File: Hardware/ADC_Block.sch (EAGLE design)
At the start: 33 parts, among them U1 ADS1015, U2 PCA9306, U3 3.3V

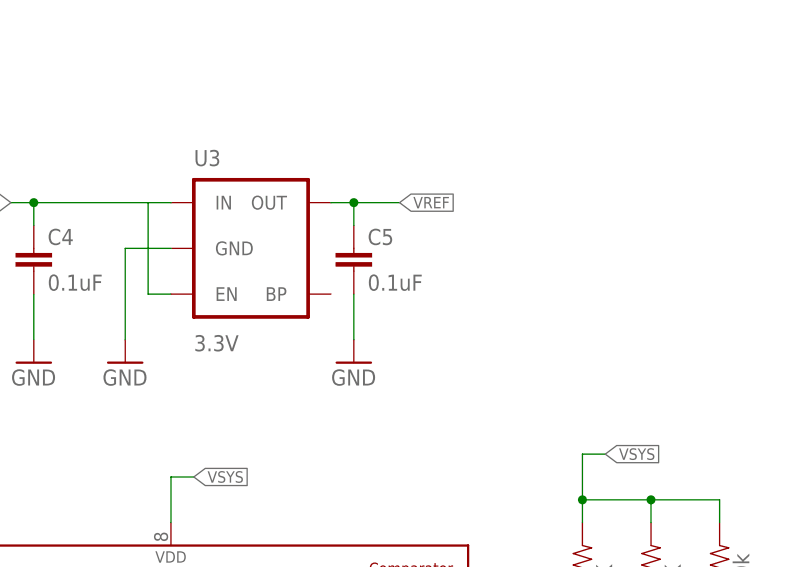
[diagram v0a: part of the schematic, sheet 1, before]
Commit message: replaces output capacitor on the 3.3v regulator with 2.2uF
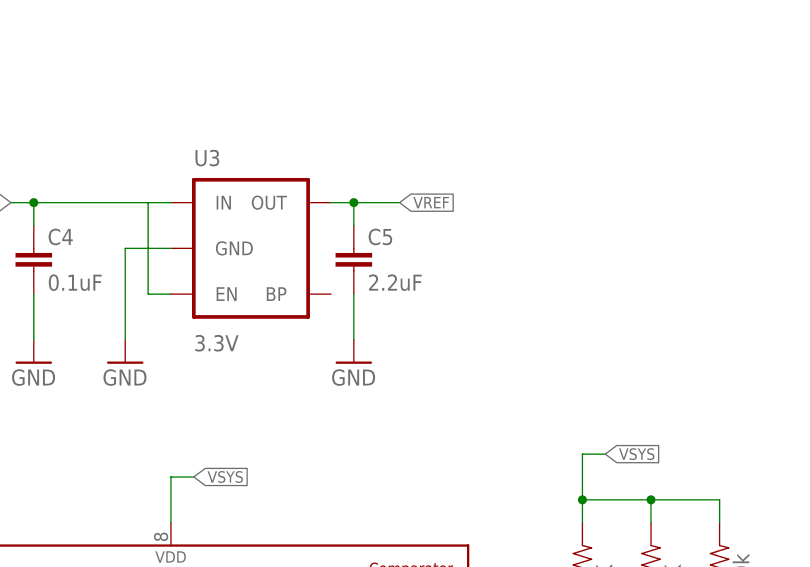
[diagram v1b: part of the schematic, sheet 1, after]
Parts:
- C5: value 0.1uF -> 2.2uF; device SparkFun-Capacitors:0.1UF-25V(+80/-20%)(0603) -> SparkFun-Capacitors:2.2UF-10V-20%(0603)
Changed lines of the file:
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@@
 <?xml version="1.0" encoding="utf-8"?>
 <!DOCTYPE eagle SYSTEM "eagle.dtd">
-<eagle version="7.3.0">
+<eagle version="7.1.0">
 <drawing>
 <settings>
@@
 <part name="U3" library="SparkFun-PowerIC" deviceset="MIC5205" device="3.3V" value="3.3V"/>
 <part name="C4" library="SparkFun-Capacitors" deviceset="0.1UF-25V(+80/-20%)(0603)" device="" value="0.1uF"/>
-<part name="C5" library="SparkFun-Capacitors" deviceset="0.1UF-25V(+80/-20%)(0603)" device="" value="0.1uF"/>
+<part name="C5" library="SparkFun-Capacitors" deviceset="2.2UF-10V-20%(0603)" device="" value="2.2uF"/>
 <part name="GND8" library="SparkFun-Aesthetics" deviceset="GND" device=""/>
 <part name="GND9" library="SparkFun-Aesthetics" deviceset="GND" device=""/>

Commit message: fixed thermal issue preventing gnd pour to connect with pads
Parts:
- FRAME1, FRAME2: value (none) -> FRAME-LETTER

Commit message: updated part values
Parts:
- R1, R2: device SparkFun-Resistors:10KOHM1/10W1%(0603)0603 -> SparkFun-Resistors:10KOHM-1/10W-1%(0603)0603
- R4, R5, R6: device SparkFun-Resistors:2.2KOHM1/10W1%(0603) -> SparkFun-Resistors:2.2KOHM-1/10W-1%(0603)
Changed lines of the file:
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@@
 <part name="C1" library="SparkFun-Capacitors" deviceset="0.1UF-25V(+80/-20%)(0603)" device="" value="0.1uF"/>
 <part name="U1" library="SparkFun-AnalogIC" deviceset="ADS1015" device="" value="ADS1015"/>
-<part name="R1" library="SparkFun-Resistors" deviceset="10KOHM1/10W1%(0603)" device="0603" value="10K"/>
-<part name="R2" library="SparkFun-Resistors" deviceset="10KOHM1/10W1%(0603)" device="0603" value="10K"/>
+<part name="R1" library="SparkFun-Resistors" deviceset="10KOHM-1/10W-1%(0603)" device="0603" value="10K"/>
+<part name="R2" library="SparkFun-Resistors" deviceset="10KOHM-1/10W-1%(0603)" device="0603" value="10K"/>
 <part name="U2" library="SparkFun-DigitalIC" deviceset="PCA9306" device="PCA9306DC-1:1" value="PCA9306"/>
 <part name="SUPPLY1" library="SparkFun-Aesthetics" deviceset="1.8V" device=""/>
@@
 <part name="SUPPLY4" library="SparkFun-Aesthetics" deviceset="1.8V" device=""/>
 <part name="R3" library="SparkFun-Resistors" deviceset="200KOHM1/10W1%(0603)" device="200K" value="200k"/>
-<part name="R4" library="SparkFun-Resistors" deviceset="2.2KOHM1/10W1%(0603)" device="" value="DNP"/>
-<part name="R5" library="SparkFun-Resistors" deviceset="2.2KOHM1/10W1%(0603)" device="" value="DNP"/>
+<part name="R4" library="SparkFun-Resistors" deviceset="2.2KOHM-1/10W-1%(0603)" device="" value="DNP"/>
+<part name="R5" library="SparkFun-Resistors" deviceset="2.2KOHM-1/10W-1%(0603)" device="" value="DNP"/>
 <part name="GND2" library="SparkFun-Aesthetics" deviceset="GND" device=""/>
 <part name="GND5" library="SparkFun-Aesthetics" deviceset="GND" device=""/>
@@
 <part name="LOGO1" library="SparkFun-Aesthetics" deviceset="SFE_LOGO_NAME_FLAME" device=".1_INCH"/>
 <part name="LOGO4" library="SparkFun-Aesthetics" deviceset="OSHW-LOGO" device="S"/>
-<part name="R6" library="SparkFun-Resistors" deviceset="2.2KOHM1/10W1%(0603)" device="" value="2.2k"/>
+<part name="R6" library="SparkFun-Resistors" deviceset="2.2KOHM-1/10W-1%(0603)" device="" value="2.2k"/>
 <part name="FID1" library="SparkFun-Aesthetics" deviceset="FIDUCIAL" device="1X2" value="FIDUCIAL1X2"/>
 <part name="FID2" library="SparkFun-Aesthetics" deviceset="FIDUCIAL" device="1X2" value="FIDUCIAL1X2"/>
@@
 <junction x="78.74" y="149.86"/>
 <label x="76.2" y="149.86" size="1.27" layer="95" rot="R180" xref="yes"/>
+<junction x="91.44" y="149.86"/>
 </segment>
 </net>
@@
 </sheet>
 </sheets>
+<errors>
+</errors>
 </schematic>
 </drawing>

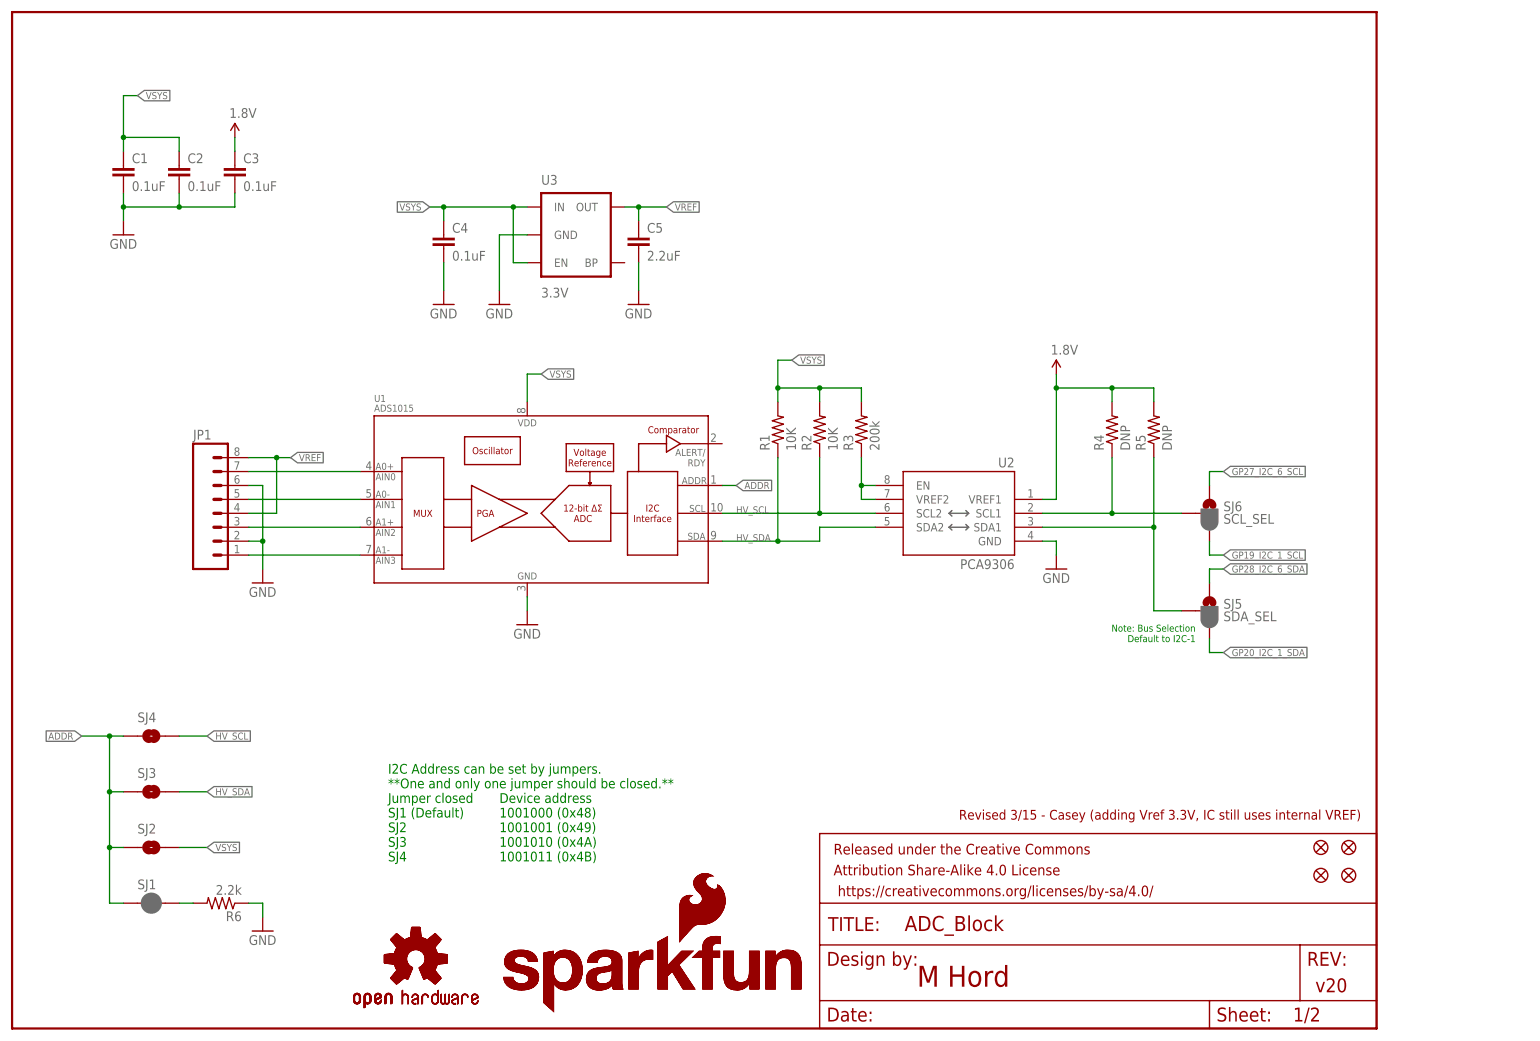
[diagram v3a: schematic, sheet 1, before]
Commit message: Added resistor to output cap on LDO. Changed header to locking male header.
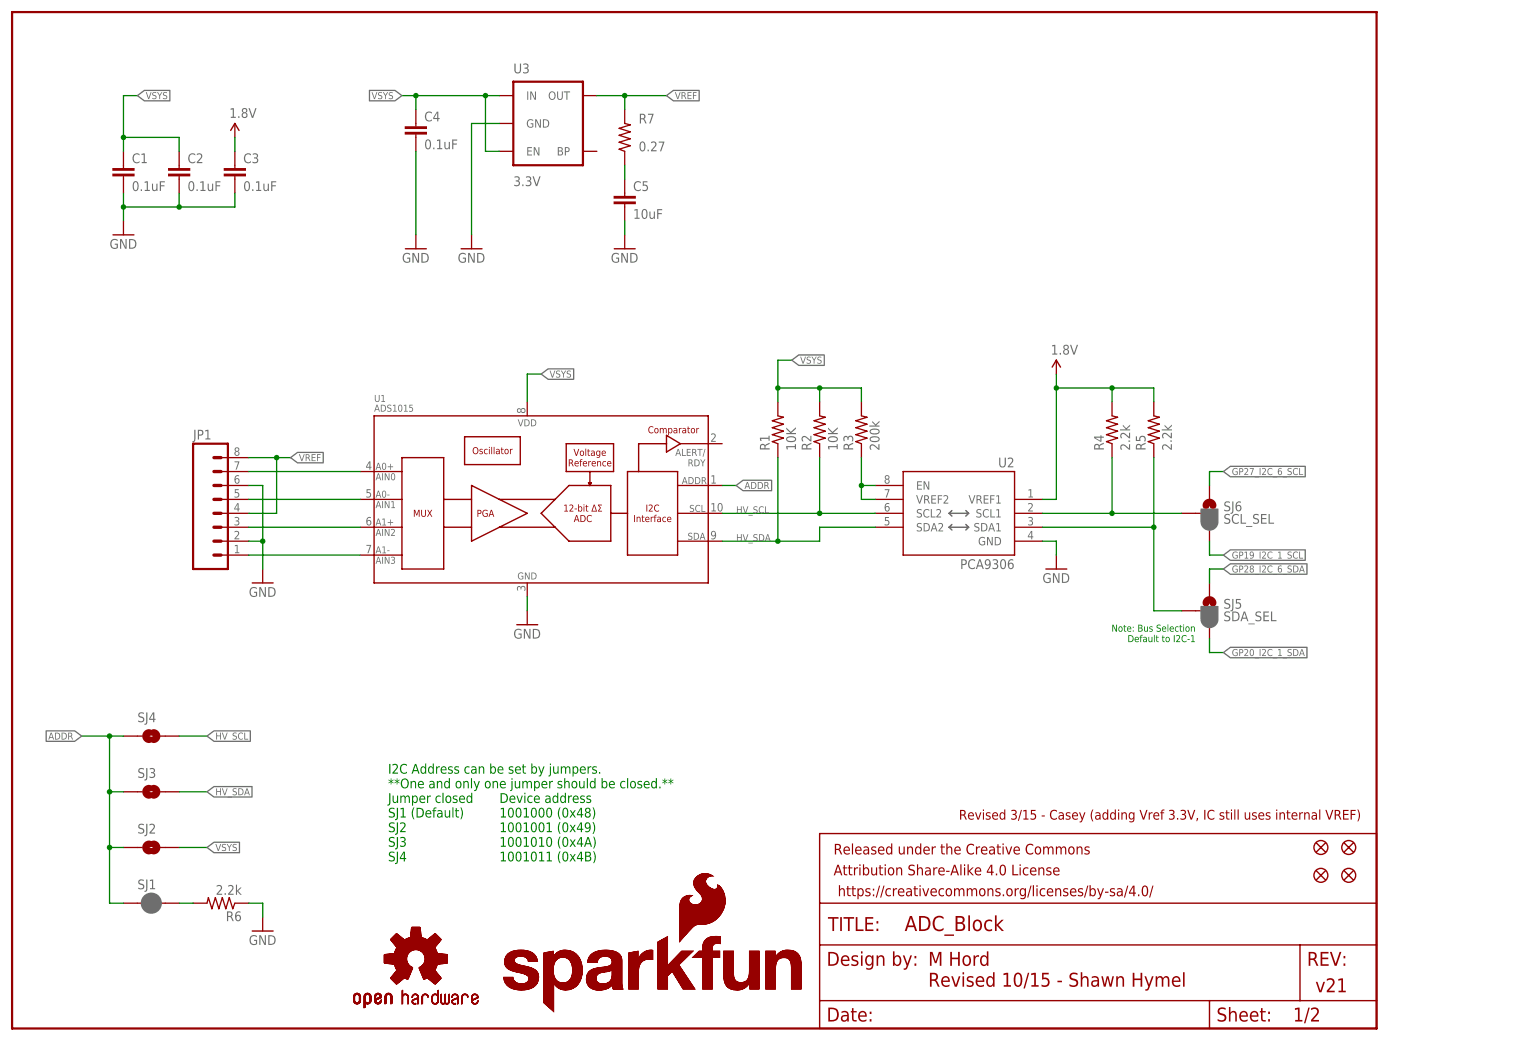
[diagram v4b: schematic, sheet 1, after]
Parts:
- added R7: 0.27, SparkFun-Resistors:0.27OHM-1/10W-1%(0603)
- C5: value 2.2uF -> 10uF; device SparkFun-Capacitors:2.2UF-10V-20%(0603) -> SparkFun-Capacitors:10UF10V10%(0805)
- JP1: device SparkFun-Connectors:M08 -> SparkFun-Connectors:M08LOCK
- R4, R5: value DNP -> 2.2k
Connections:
- new net N$5: C5.1, R7.1
- net VREF: now also R7.2; no longer C5.1
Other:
- note added: "Revised 10/15 - Shawn Hymel"
- note added: "v21"
- note removed: "v20"
- moved on the sheet: C4, C5, U3
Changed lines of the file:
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@@
 <?xml version="1.0" encoding="utf-8"?>
 <!DOCTYPE eagle SYSTEM "eagle.dtd">
-<eagle version="7.1.0">
+<eagle version="7.2.0">
 <drawing>
 <settings>
@@
 <setting verticaltext="up"/>
 </settings>
-<grid distance="0.1" unitdist="inch" unit="inch" style="lines" multiple="1" display="no" altdistance="0.01" altunitdist="inch" altunit="inch"/>
+<grid distance="0.1" unitdist="inch" unit="inch" style="lines" multiple="1" display="yes" altdistance="0.01" altunitdist="inch" altunit="inch"/>
 <layers>
 <layer number="1" name="Top" color="4" fill="1" visible="no" active="no"/>
@@
 <layer number="113" name="IDFDebug" color="4" fill="1" visible="yes" active="yes"/>
 <layer number="114" name="Badge_Outline" color="11" fill="1" visible="no" active="no"/>
+<layer number="115" name="ReferenceISLANDS" color="7" fill="1" visible="yes" active="yes"/>
 <layer number="116" name="Patch_BOT" color="9" fill="4" visible="yes" active="yes"/>
 <layer number="118" name="Rect_Pads" color="7" fill="1" visible="yes" active="yes"/>
@@
 <part name="SUPPLY4" library="SparkFun-Aesthetics" deviceset="1.8V" device=""/>
 <part name="R3" library="SparkFun-Resistors" deviceset="200KOHM1/10W1%(0603)" device="200K" value="200k"/>
-<part name="R4" library="SparkFun-Resistors" deviceset="2.2KOHM-1/10W-1%(0603)" device="" value="DNP"/>
-<part name="R5" library="SparkFun-Resistors" deviceset="2.2KOHM-1/10W-1%(0603)" device="" value="DNP"/>
+<part name="R4" library="SparkFun-Resistors" deviceset="2.2KOHM-1/10W-1%(0603)" device="" value="2.2k"/>
+<part name="R5" library="SparkFun-Resistors" deviceset="2.2KOHM-1/10W-1%(0603)" device="" value="2.2k"/>
 <part name="GND2" library="SparkFun-Aesthetics" deviceset="GND" device=""/>
 <part name="GND5" library="SparkFun-Aesthetics" deviceset="GND" device=""/>
 <part name="GND6" library="SparkFun-Aesthetics" deviceset="GND" device=""/>
-<part name="JP1" library="SparkFun-Connectors" deviceset="M08" device=""/>
+<part name="JP1" library="SparkFun-Connectors" deviceset="M08" device="LOCK"/>
 <part name="GND7" library="SparkFun-Aesthetics" deviceset="GND" device=""/>
 <part name="LOGO1" library="SparkFun-Aesthetics" deviceset="SFE_LOGO_NAME_FLAME" device=".1_INCH"/>
@@
 <part name="U3" library="SparkFun-PowerIC" deviceset="MIC5205" device="3.3V" value="3.3V"/>
 <part name="C4" library="SparkFun-Capacitors" deviceset="0.1UF-25V(+80/-20%)(0603)" device="" value="0.1uF"/>
-<part name="C5" library="SparkFun-Capacitors" deviceset="2.2UF-10V-20%(0603)" device="" value="2.2uF"/>
+<part name="C5" library="SparkFun-Capacitors" deviceset="10UF10V10%(0805)" device="" value="10uF"/>
 <part name="GND8" library="SparkFun-Aesthetics" deviceset="GND" device=""/>
 <part name="GND9" library="SparkFun-Aesthetics" deviceset="GND" device=""/>
@@
 <part name="SJ5" library="SparkFun-Passives" deviceset="JUMPER-PAD-3-2OF3_NC_BY_PASTE" device="" value="SDA_SEL"/>
 <part name="SJ6" library="SparkFun-Passives" deviceset="JUMPER-PAD-3-2OF3_NC_BY_PASTE" device="" value="SCL_SEL"/>
+<part name="R7" library="SparkFun-Resistors" deviceset="0.27OHM-1/10W-1%(0603)" device="" value="0.27"/>
 </parts>
 <sheets>
@@
 1001010 (0x4A)
 1001011 (0x4B)</text>
-<text x="237.744" y="6.604" size="2.54" layer="94">v20</text>
-<text x="165.1" y="7.62" size="3.81" layer="94">M Hord</text>
+<text x="237.744" y="6.604" size="2.54" layer="94">v21</text>
+<text x="167.132" y="11.43" size="2.54" layer="94">M Hord</text>
 <text x="172.72" y="38.1" size="1.778" layer="94">Revised 3/15 - Casey (adding Vref 3.3V, IC still uses internal VREF)</text>
 <text x="215.9" y="73.66" size="1.27" layer="91" rot="R180">Note: Bus Selection
 Default to I2C-1</text>
+<text x="167.132" y="7.62" size="2.54" layer="94">Revised 10/15 - Shawn Hymel</text>
 </plain>
 <instances>
@@
 <instance part="FID3" gate="G$1" x="238.76" y="33.02"/>
 <instance part="FID4" gate="G$1" x="243.84" y="33.02"/>
-<instance part="U3" gate="G$1" x="104.14" y="144.78"/>
-<instance part="C4" gate="G$1" x="78.74" y="142.24"/>
-<instance part="C5" gate="G$1" x="114.3" y="142.24"/>
-<instance part="GND8" gate="1" x="78.74" y="132.08"/>
-<instance part="GND9" gate="1" x="88.9" y="132.08"/>
-<instance part="GND10" gate="1" x="114.3" y="132.08"/>
+<instance part="U3" gate="G$1" x="99.06" y="165.1"/>
+<instance part="C4" gate="G$1" x="73.66" y="162.56"/>
+<instance part="C5" gate="G$1" x="111.76" y="149.86"/>
+<instance part="GND8" gate="1" x="73.66" y="142.24"/>
+<instance part="GND9" gate="1" x="83.82" y="142.24"/>
+<instance part="GND10" gate="1" x="111.76" y="142.24"/>
 <instance part="SJ5" gate="G$1" x="218.44" y="76.2"/>
 <instance part="SJ6" gate="G$1" x="218.44" y="93.98"/>
+<instance part="R7" gate="G$1" x="111.76" y="162.56" smashed="yes" rot="R90">
+<attribute name="NAME" x="114.3" y="165.1" size="1.778" layer="95"/>
+<attribute name="VALUE" x="114.3" y="160.02" size="1.778" layer="96"/>
+</instance>
 </instances>
 <busses>
@@
 <pinref part="C4" gate="G$1" pin="2"/>
 <pinref part="GND8" gate="1" pin="GND"/>
-<wire x1="78.74" y1="134.62" x2="78.74" y2="139.7" width="0.1524" layer="91"/>
+<wire x1="73.66" y1="144.78" x2="73.66" y2="160.02" width="0.1524" layer="91"/>
 </segment>
 <segment>
 <pinref part="U3" gate="G$1" pin="GND"/>
 <pinref part="GND9" gate="1" pin="GND"/>
-<wire x1="93.98" y1="144.78" x2="88.9" y2="144.78" width="0.1524" layer="91"/>
-<wire x1="88.9" y1="144.78" x2="88.9" y2="134.62" width="0.1524" layer="91"/>
+<wire x1="88.9" y1="165.1" x2="83.82" y2="165.1" width="0.1524" layer="91"/>
+<wire x1="83.82" y1="165.1" x2="83.82" y2="144.78" width="0.1524" layer="91"/>
 </segment>
 <segment>
 <pinref part="C5" gate="G$1" pin="2"/>
 <pinref part="GND10" gate="1" pin="GND"/>
-<wire x1="114.3" y1="134.62" x2="114.3" y2="139.7" width="0.1524" layer="91"/>
+<wire x1="111.76" y1="144.78" x2="111.76" y2="147.32" width="0.1524" layer="91"/>
 </segment>
 </net>
@@
 <segment>
 <pinref part="U3" gate="G$1" pin="EN"/>
-<wire x1="93.98" y1="139.7" x2="91.44" y2="139.7" width="0.1524" layer="91"/>
-<wire x1="91.44" y1="139.7" x2="91.44" y2="149.86" width="0.1524" layer="91"/>
+<wire x1="88.9" y1="160.02" x2="86.36" y2="160.02" width="0.1524" layer="91"/>
+<wire x1="86.36" y1="160.02" x2="86.36" y2="170.18" width="0.1524" layer="91"/>
 <pinref part="U3" gate="G$1" pin="IN"/>
-<wire x1="91.44" y1="149.86" x2="93.98" y2="149.86" width="0.1524" layer="91"/>
-<wire x1="91.44" y1="149.86" x2="78.74" y2="149.86" width="0.1524" layer="91"/>
-<wire x1="78.74" y1="149.86" x2="78.74" y2="147.32" width="0.1524" layer="91"/>
+<wire x1="86.36" y1="170.18" x2="88.9" y2="170.18" width="0.1524" layer="91"/>
+<wire x1="86.36" y1="170.18" x2="73.66" y2="170.18" width="0.1524" layer="91"/>
+<wire x1="73.66" y1="170.18" x2="73.66" y2="167.64" width="0.1524" layer="91"/>
 <pinref part="C4" gate="G$1" pin="1"/>
-<wire x1="78.74" y1="149.86" x2="76.2" y2="149.86" width="0.1524" layer="91"/>
-<junction x="78.74" y="149.86"/>
-<label x="76.2" y="149.86" size="1.27" layer="95" rot="R180" xref="yes"/>
-<junction x="91.44" y="149.86"/>
+<wire x1="73.66" y1="170.18" x2="71.12" y2="170.18" width="0.1524" layer="91"/>
+<junction x="73.66" y="170.18"/>
+<label x="71.12" y="170.18" size="1.27" layer="95" rot="R180" xref="yes"/>
+<junction x="86.36" y="170.18"/>
 </segment>
 </net>
@@
 <segment>
 <pinref part="U3" gate="G$1" pin="OUT"/>
-<pinref part="C5" gate="G$1" pin="1"/>
-<wire x1="111.76" y1="149.86" x2="114.3" y2="149.86" width="0.1524" layer="91"/>
-<wire x1="114.3" y1="149.86" x2="114.3" y2="147.32" width="0.1524" layer="91"/>
-<wire x1="114.3" y1="149.86" x2="119.38" y2="149.86" width="0.1524" layer="91"/>
-<junction x="114.3" y="149.86"/>
-<label x="119.38" y="149.86" size="1.27" layer="95" xref="yes"/>
+<wire x1="106.68" y1="170.18" x2="111.76" y2="170.18" width="0.1524" layer="91"/>
+<label x="119.38" y="170.18" size="1.27" layer="95" xref="yes"/>
+<pinref part="R7" gate="G$1" pin="2"/>
+<wire x1="111.76" y1="170.18" x2="119.38" y2="170.18" width="0.1524" layer="91"/>
+<wire x1="111.76" y1="170.18" x2="111.76" y2="167.64" width="0.1524" layer="91"/>
+<junction x="111.76" y="170.18"/>
 </segment>
 </net>
@@
 </segment>
 </net>
+<net name="N$5" class="0">
+<segment>
+<pinref part="R7" gate="G$1" pin="1"/>
+<pinref part="C5" gate="G$1" pin="1"/>
+<wire x1="111.76" y1="157.48" x2="111.76" y2="154.94" width="0.1524" layer="91"/>
+</segment>
+</net>
